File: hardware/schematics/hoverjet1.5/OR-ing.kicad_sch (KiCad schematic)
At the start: 9 parts, among them Q1 BSC070N10NS5, U1 LM5050-1

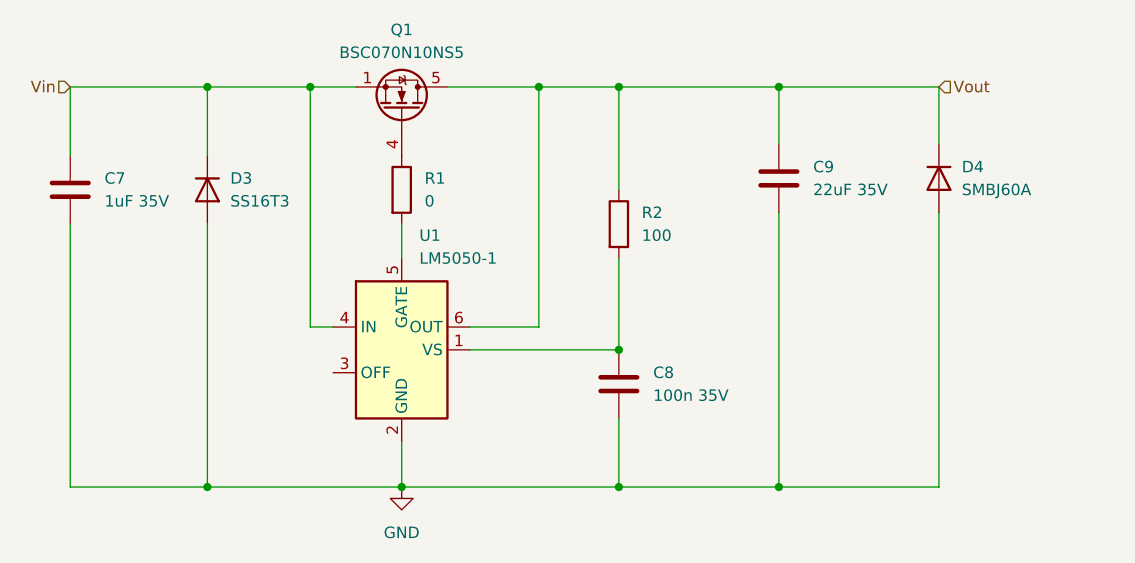
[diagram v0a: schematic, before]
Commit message: added part numbers, manufacturers, and relevant parameters to OR-ing sheet components
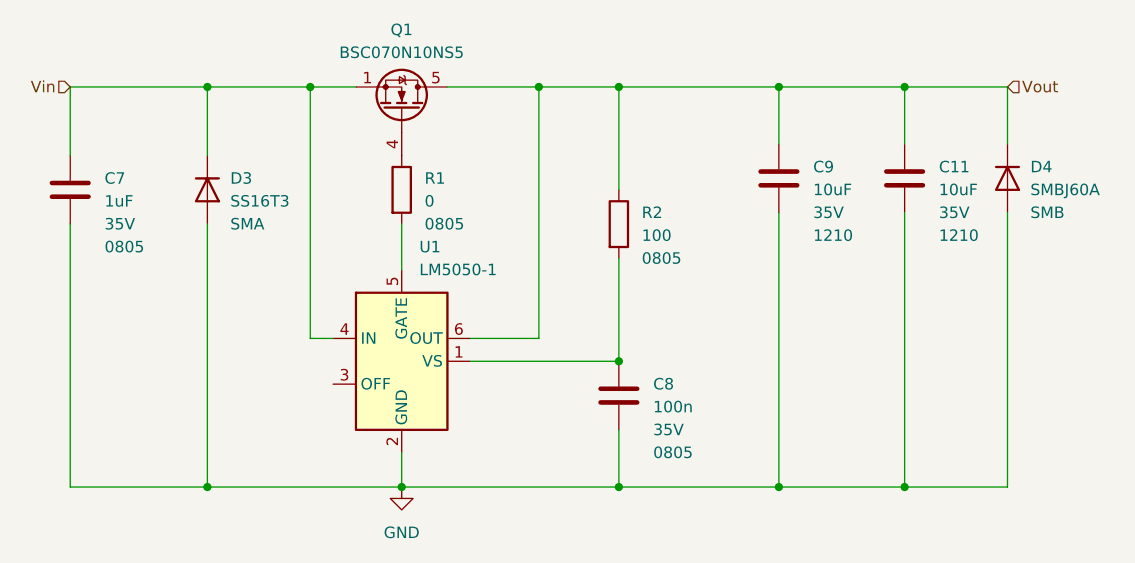
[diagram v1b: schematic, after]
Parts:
- added C11: 10uF, Capacitor_SMD:C_1210_3225Metric_Pad1.33x2.70mm_HandSolder, symbol Device:C
- C7: value 1uF 35V -> 1uF; MN (none) -> Murata; PN (none) -> GRM219R7YA105MA12D; Package (none) -> 0805; VDC (none) -> 35V
- C8: value 100n 35V -> 100n; MN (none) -> Samsung; PN (none) -> CL10B104KB8NNNL; Package (none) -> 0805; VDC (none) -> 35V
- C9: value 22uF 35V -> 10uF; footprint (none) -> Capacitor_SMD:C_1210_3225Metric_Pad1.33x2.70mm_HandSolder; MN (none) -> Samsung; PN (none) -> CL32B106KLJNNNE; Package (none) -> 1210; VDC (none) -> 35V
- D3: MN (none) -> Onsemi; PN (none) -> SS16T3; Package (none) -> SMA
- D4: MN (none) -> Bourns; PN (none) -> SMBJ60A; Package (none) -> SMB
- Q1: MN (none) -> Infineon; PN (none) -> BSC070N10NS5ATMA1
- R1: Package (none) -> 0805; Tolerance (none) -> 1%
- R2: MN (none) -> Panasonic; PN (none) -> ERJ-6ENF1000V; Package (none) -> 0805; Tolerance (none) -> 1%
- U1: MN (none) -> Texas Instruments; PN (none) -> LM5050MK-1; Package (none) -> SOT-23-6
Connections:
- net GND: now also C11.2
- net Vout: now also C11.1
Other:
- moved on the sheet: C8, D4, U1
